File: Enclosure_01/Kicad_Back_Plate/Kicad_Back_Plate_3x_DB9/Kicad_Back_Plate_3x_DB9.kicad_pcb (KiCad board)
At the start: 2 copper layers, 124.8 x 50.9 mm, 0 parts

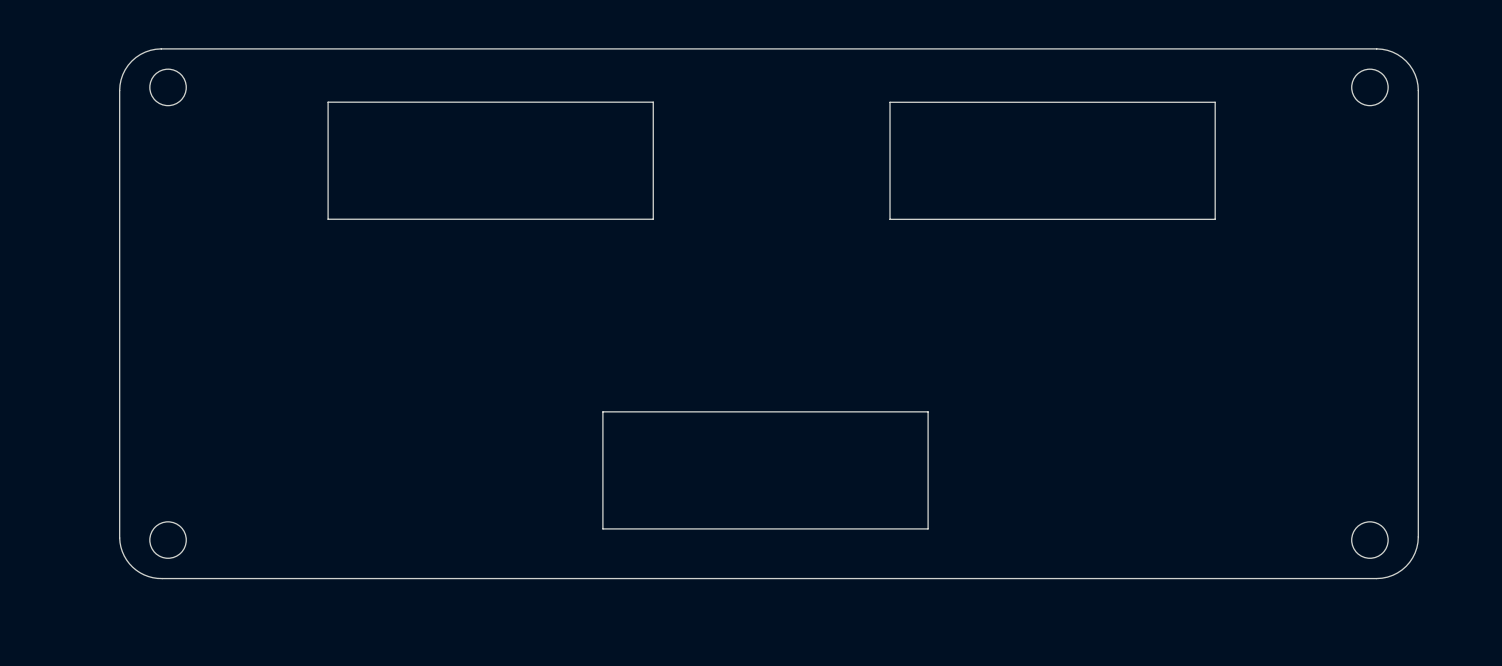
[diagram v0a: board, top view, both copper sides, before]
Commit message: Added masks to Kicad Front/back plates
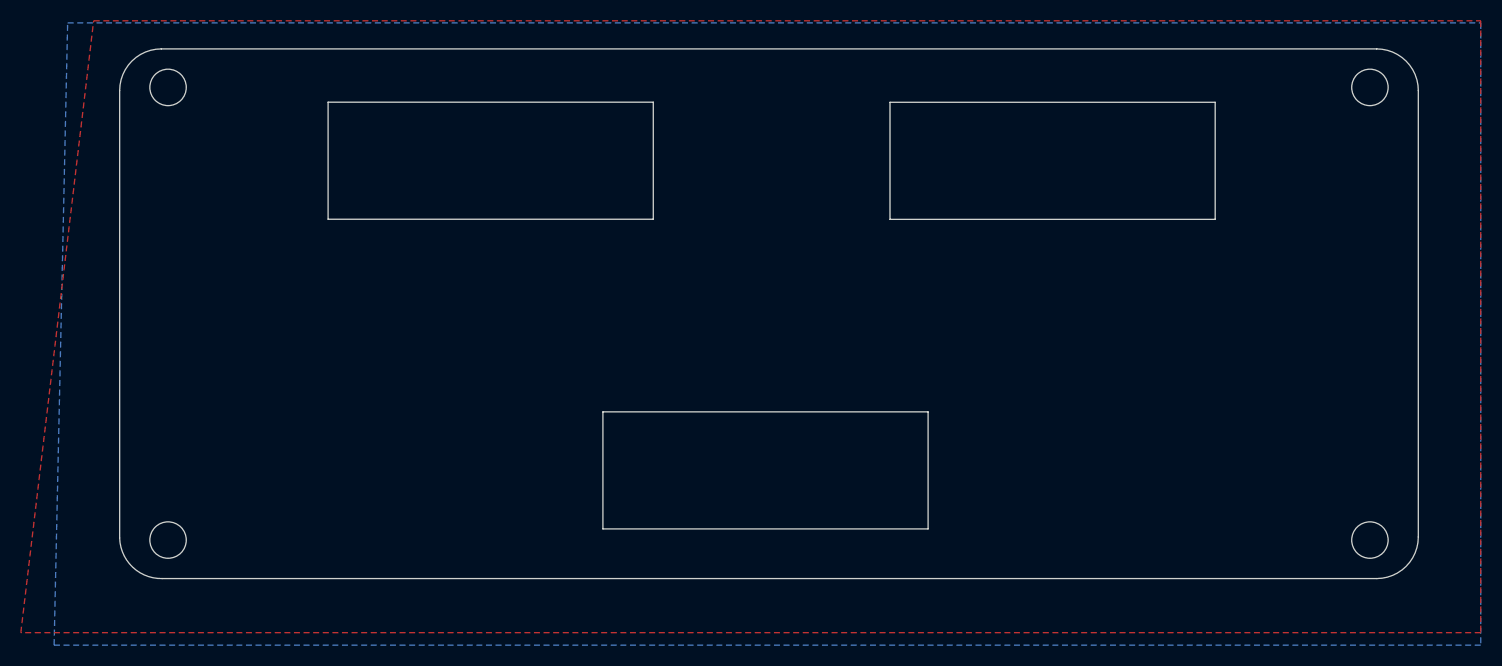
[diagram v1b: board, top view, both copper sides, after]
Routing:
- added copper zone on B.Cu, net (none)
- added copper zone on F.Cu, net (none)
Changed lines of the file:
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@@
     (pad_to_mask_clearance 0)
     (aux_axis_origin 0 0)
-    (visible_elements FFFFFF7F)
+    (visible_elements 7FFFFFFF)
     (pcbplotparams
       (layerselection 0x010fc_ffffffff)
@@
   (gr_line (start 20.03 5.12) (end 51.28 5.12) (layer Edge.Cuts) (width 0.05))
   (gr_arc (start 120.8 46.9) (end 120.8 50.9) (angle -90) (layer Edge.Cuts) (width 0.05))
+  (zone (net 0) (net_name "") (layer F.Cu) (hatch edge 0.508)
+    (connect_pads (clearance 0.508))
+    (min_thickness 0.254)
+    (fill yes (arc_segments 32) (thermal_gap 0.508) (thermal_bridge_width 0.508))
+    (polygon
+      (pts
+        (xy 130.8 56.1) (xy -9.5 56.1) (xy -2.5 -2.7) (xy 130.8 -2.7)
+      )
+    )
+  )
+  (zone (net 0) (net_name "") (layer B.Cu) (hatch edge 0.508)
+    (connect_pads (clearance 0.508))
+    (min_thickness 0.254)
+    (fill yes (arc_segments 32) (thermal_gap 0.508) (thermal_bridge_width 0.508))
+    (polygon
+      (pts
+        (xy 130.8 57.3) (xy -6.3 57.3) (xy -5 -2.5) (xy 130.8 -2.5)
+      )
+    )
+  )
 )

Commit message: Updated mounting holes for Copper Plane and Gerber
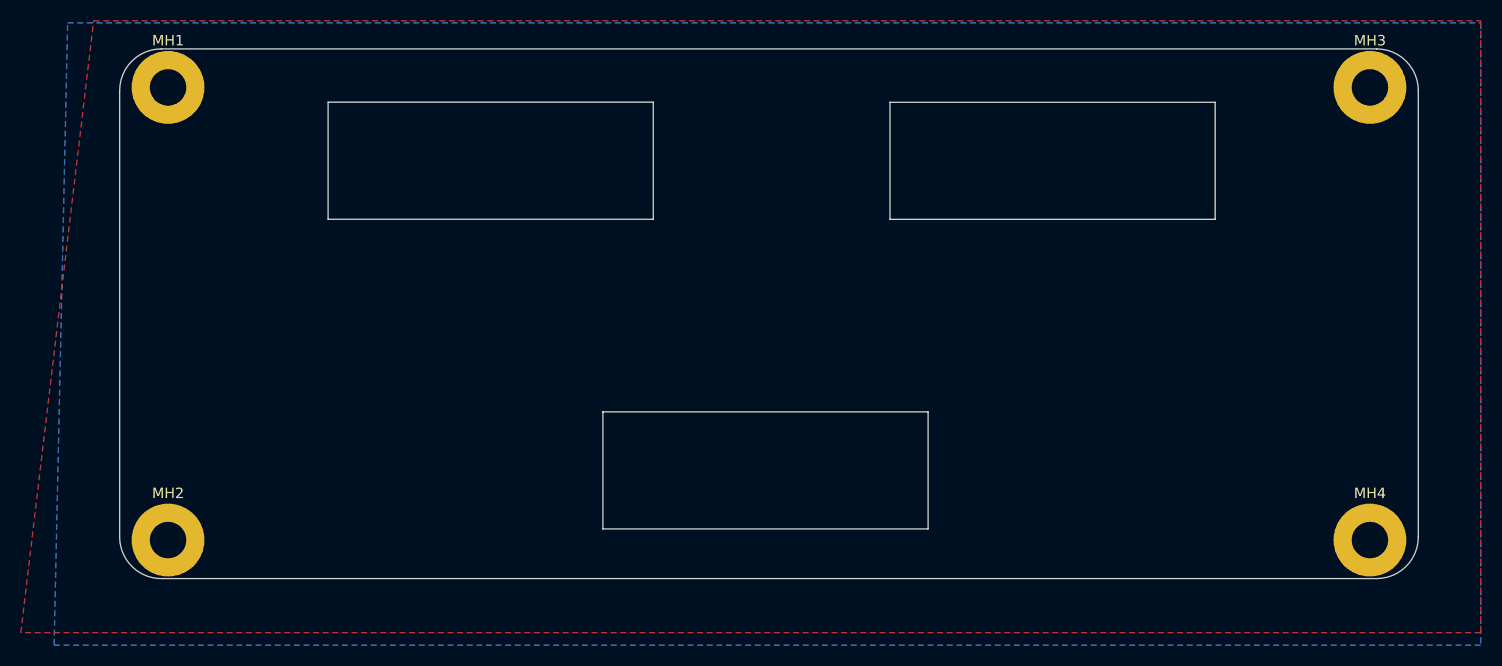
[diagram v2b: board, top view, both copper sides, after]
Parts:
- added MH1: MountingHole, MountingHole:MountingHole_3.5mm_Pad, F.Cu at (4.65, 3.70)
- added MH2: MountingHole, MountingHole:MountingHole_3.5mm_Pad, F.Cu at (4.65, 47.2)
- added MH3: MountingHole, MountingHole:MountingHole_3.5mm_Pad, F.Cu at (120.2, 3.70)
- added MH4: MountingHole, MountingHole:MountingHole_3.5mm_Pad, F.Cu at (120.2, 47.2)
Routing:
- added copper zone on B.Cu, net GND
- added copper zone on F.Cu, net GND
- removed copper zone on B.Cu, net (none)
- removed copper zone on F.Cu, net (none)
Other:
- outline, holes or cut-outs redrawn
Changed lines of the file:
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@@
   (general
     (thickness 1.6)
-    (drawings 24)
+    (drawings 20)
     (tracks 0)
     (zones 0)
-    (modules 0)
-    (nets 1)
+    (modules 4)
+    (nets 2)
   )
   (page A4)
@@
     (pcbplotparams
       (layerselection 0x010fc_ffffffff)
-      (usegerberextensions false)
-      (usegerberattributes true)
-      (usegerberadvancedattributes true)
-      (creategerberjobfile true)
+      (usegerberextensions true)
+      (usegerberattributes false)
+      (usegerberadvancedattributes false)
+      (creategerberjobfile false)
       (excludeedgelayer true)
       (linewidth 0.100000)
@@
       (psa4output false)
       (plotreference true)
-      (plotvalue true)
+      (plotvalue false)
       (plotinvisibletext false)
       (padsonsilk false)
-      (subtractmaskfromsilk false)
+      (subtractmaskfromsilk true)
       (outputformat 1)
       (mirror false)
@@
   )
   (net 0 "")
+  (net 1 GND)
   (net_class Default "This is the default net class."
     (clearance 0.2)
@@
     (uvia_dia 0.3)
     (uvia_drill 0.1)
+    (add_net GND)
+  )
+  (module MountingHole:MountingHole_3.5mm_Pad (layer F.Cu)
+    (at 4.65 3.7)
+    (descr "Mounting Hole 3.5mm")
+    (tags "mounting hole 3.5mm")
+    (attr virtual)
+    (fp_text reference MH1 (at 0 -4.5) (layer F.SilkS)
+      (effects (font (size 1 1) (thickness 0.15)))
+    )
+    (fp_text value MountingHole (at 0 4.5) (layer F.Fab)
+      (effects (font (size 1 1) (thickness 0.15)))
+    )
+    (fp_circle (center 0 0) (end 3.75 0) (layer F.CrtYd) (width 0.05))
+    (fp_circle (center 0 0) (end 3.5 0) (layer Cmts.User) (width 0.15))
+    (fp_text user %R (at 0.3 0) (layer F.Fab)
+      (effects (font (size 1 1) (thickness 0.15)))
+    )
+    (pad 1 thru_hole circle (at 0 0) (size 7 7) (drill 3.5) (layers *.Cu *.Mask)
+      (net 1 GND))
+  )
+  (module MountingHole:MountingHole_3.5mm_Pad (layer F.Cu)
+    (at 4.65 47.2)
+    (descr "Mounting Hole 3.5mm")
+    (tags "mounting hole 3.5mm")
+    (attr virtual)
+    (fp_text reference MH2 (at 0 -4.5) (layer F.SilkS)
+      (effects (font (size 1 1) (thickness 0.15)))
+    )
+    (fp_text value MountingHole (at 0 4.5) (layer F.Fab)
+      (effects (font (size 1 1) (thickness 0.15)))
+    )
+    (fp_text user %R (at 0.3 0) (layer F.Fab)
+      (effects (font (size 1 1) (thickness 0.15)))
+    )
+    (fp_circle (center 0 0) (end 3.5 0) (layer Cmts.User) (width 0.15))
+    (fp_circle (center 0 0) (end 3.75 0) (layer F.CrtYd) (width 0.05))
+    (pad 1 thru_hole circle (at 0 0) (size 7 7) (drill 3.5) (layers *.Cu *.Mask)
+      (net 1 GND))
+  )
+  (module MountingHole:MountingHole_3.5mm_Pad (layer F.Cu)
+    (at 120.15 3.7)
+    (descr "Mounting Hole 3.5mm")
+    (tags "mounting hole 3.5mm")
+    (attr virtual)
+    (fp_text reference MH3 (at 0 -4.5) (layer F.SilkS)
+      (effects (font (size 1 1) (thickness 0.15)))
+    )
+    (fp_text value MountingHole (at 0 4.5) (layer F.Fab)
+      (effects (font (size 1 1) (thickness 0.15)))
+    )
+    (fp_circle (center 0 0) (end 3.75 0) (layer F.CrtYd) (width 0.05))
+    (fp_circle (center 0 0) (end 3.5 0) (layer Cmts.User) (width 0.15))
+    (fp_text user %R (at 0.3 0) (layer F.Fab)
+      (effects (font (size 1 1) (thickness 0.15)))
+    )
+    (pad 1 thru_hole circle (at 0 0) (size 7 7) (drill 3.5) (layers *.Cu *.Mask)
+      (net 1 GND))
+  )
+  (module MountingHole:MountingHole_3.5mm_Pad (layer F.Cu)
+    (at 120.15 47.2)
+    (descr "Mounting Hole 3.5mm")
+    (tags "mounting hole 3.5mm")
+    (attr virtual)
+    (fp_text reference MH4 (at 0 -4.5) (layer F.SilkS)
+      (effects (font (size 1 1) (thickness 0.15)))
+    )
+    (fp_text value MountingHole (at 0 4.5) (layer F.Fab)
+      (effects (font (size 1 1) (thickness 0.15)))
+    )
+    (fp_text user %R (at 0.3 0) (layer F.Fab)
+      (effects (font (size 1 1) (thickness 0.15)))
+    )
+    (fp_circle (center 0 0) (end 3.5 0) (layer Cmts.User) (width 0.15))
+    (fp_circle (center 0 0) (end 3.75 0) (layer F.CrtYd) (width 0.05))
+    (pad 1 thru_hole circle (at 0 0) (size 7 7) (drill 3.5) (layers *.Cu *.Mask)
+      (net 1 GND))
   )
   (gr_line (start 46.44 34.88) (end 77.69 34.88) (layer Edge.Cuts) (width 0.05))
@@
   (gr_line (start 74.03 16.38) (end 105.28 16.38) (layer Edge.Cuts) (width 0.05))
   (gr_line (start 74.03 5.13) (end 74.03 16.38) (layer Edge.Cuts) (width 0.05))
-  (gr_circle (center 120.15 47.2) (end 121.9 47.2) (layer Edge.Cuts) (width 0.05))
-  (gr_circle (center 120.15 3.7) (end 121.9 3.7) (layer Edge.Cuts) (width 0.05))
-  (gr_circle (center 4.65 47.2) (end 6.4 47.2) (layer Edge.Cuts) (width 0.05))
-  (gr_circle (center 4.65 3.7) (end 6.4 3.7) (layer Edge.Cuts) (width 0.05))
   (gr_arc (start 4 46.9) (end 0 47) (angle -90) (layer Edge.Cuts) (width 0.05))
   (gr_line (start 0 4) (end 0 47) (layer Edge.Cuts) (width 0.05))
@@
   (gr_line (start 20.03 5.12) (end 51.28 5.12) (layer Edge.Cuts) (width 0.05))
   (gr_arc (start 120.8 46.9) (end 120.8 50.9) (angle -90) (layer Edge.Cuts) (width 0.05))
-  (zone (net 0) (net_name "") (layer F.Cu) (hatch edge 0.508)
+  (zone (net 1) (net_name GND) (layer F.Cu) (hatch edge 0.508)
     (connect_pads (clearance 0.508))
     (min_thickness 0.254)
@@
     )
   )
-  (zone (net 0) (net_name "") (layer B.Cu) (hatch edge 0.508)
+  (zone (net 1) (net_name GND) (layer B.Cu) (hatch edge 0.508)
     (connect_pads (clearance 0.508))
     (min_thickness 0.254)
